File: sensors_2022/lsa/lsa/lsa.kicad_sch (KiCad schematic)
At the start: 18 parts, among them J1 Conn_01x06_Male, U1 LM324

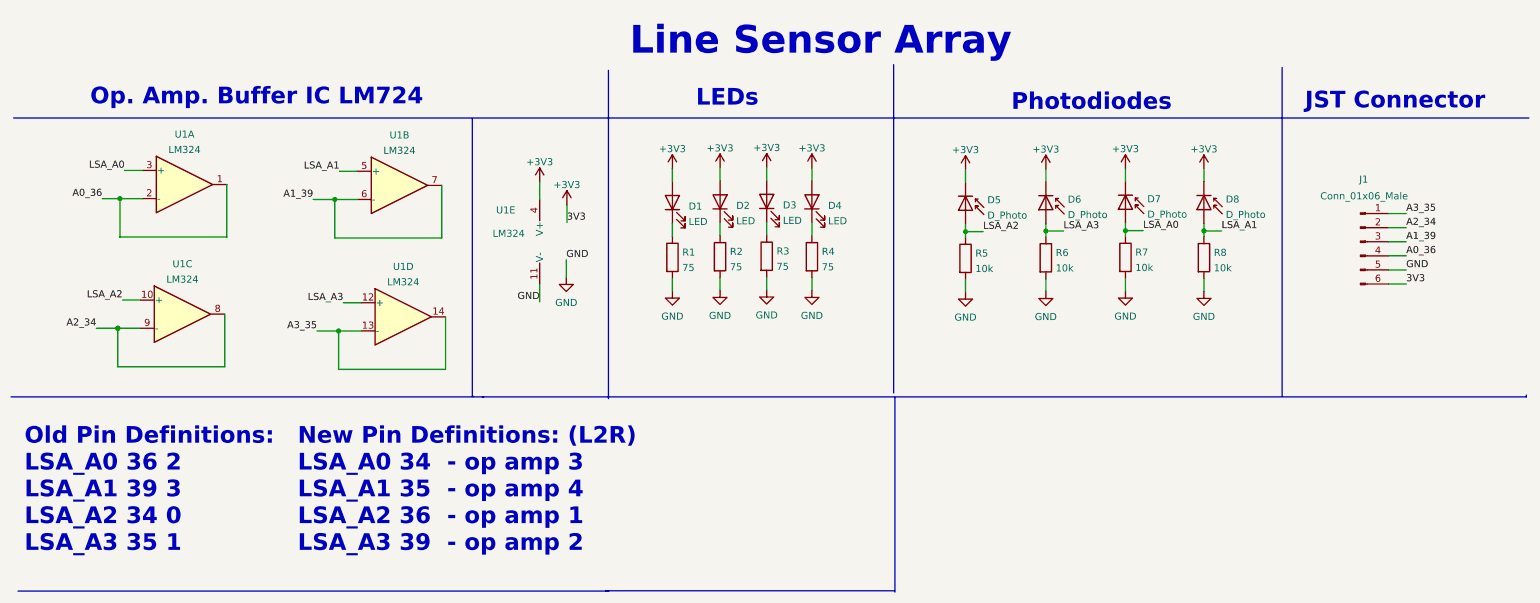
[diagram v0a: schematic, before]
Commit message: add TCRT-5000 base structure to LSA
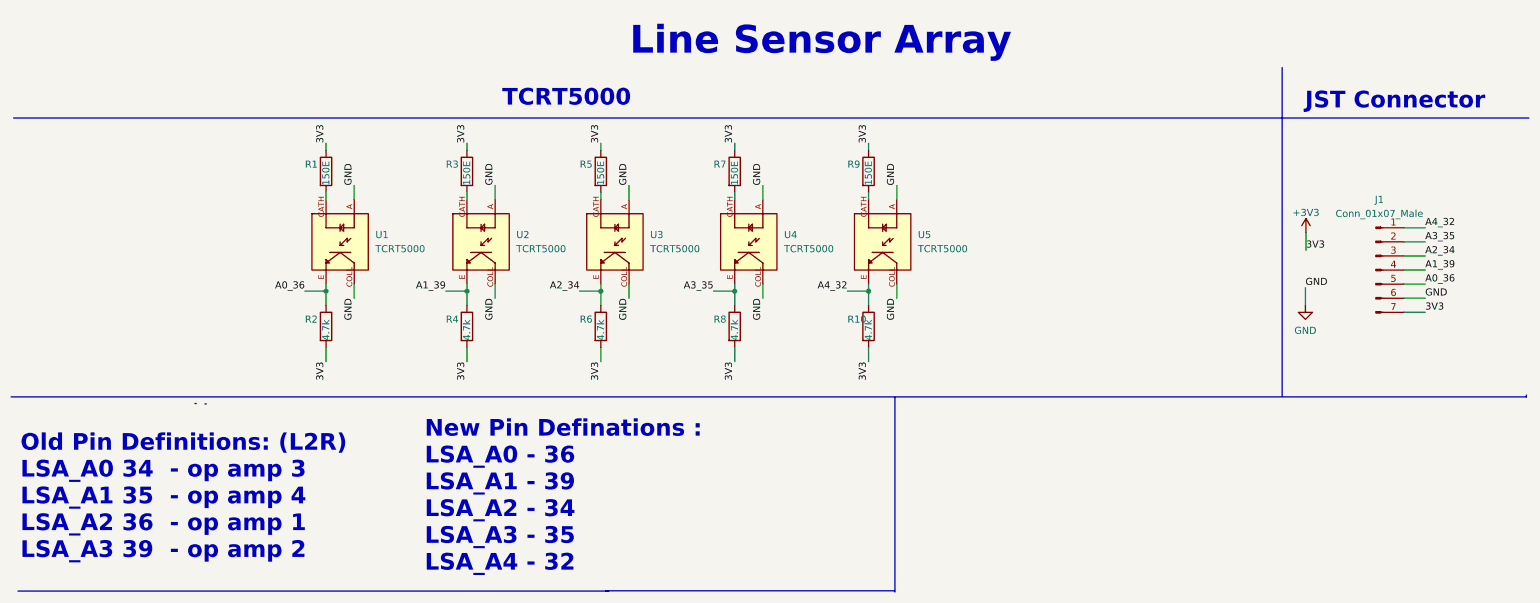
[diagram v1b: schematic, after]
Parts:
- removed D1, D2, D3, D4: LED, LED_THT:LED_D3.0mm, symbol Device:LED
- removed D5, D6, D7, D8: D_Photo, LED_THT:LED_D5.0mm, symbol Device:D_Photo
- removed J1: Conn_01x06_Male, Connector_PinSocket_2.54mm:PinSocket_1x06_P2.54mm_Vertical, symbol Connector:Conn_01x06_Male
- removed U1: LM324, Package_SO:SOIC-14_3.9x8.7mm_P1.27mm, symbol Amplifier_Operational:LM324
- added J1: Conn_01x07_Male, Connector_PinHeader_2.54mm:PinHeader_1x07_P2.54mm_Vertical, symbol Connector:Conn_01x07_Male
- added R10: 4.7k, Resistor_SMD:R_1206_3216Metric_Pad1.30x1.75mm_HandSolder, symbol Device:R
- added R9: 150E, Resistor_SMD:R_1206_3216Metric_Pad1.30x1.75mm_HandSolder, symbol Device:R
- added U1, U2, U3, U4, U5: TCRT5000, TCRT5000:OPTO_TCRT5000, symbol TCRT5000:TCRT5000
- R1, R3: value 75 -> 150E
- R2, R4: value 75 -> 4.7k
- R5, R7: value 10k -> 150E
- R6, R8: value 10k -> 4.7k
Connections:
- net LSA_A0 is gone; now on net +3V3: R7.1
- net LSA_A1 is gone; now on net A3_35: R8.1
- net LSA_A2 is gone; now on net +3V3: R5.1
- net LSA_A3 is gone; now on net A2_34: R6.1
- net +3V3: now also R1.1, R2.2, R3.1, R4.2, R6.2, R8.2, J1.7 (Pin_7), R10.2, R9.1
- net A0_36: now also R2.1, J1.5 (Pin_5), U1.E
- net A1_39: now also R4.1, J1.4 (Pin_4), U2.E
- net A2_34: now also J1.3 (Pin_3), U3.E
- net A3_35: now also J1.2 (Pin_2), U4.E
- net GND: now also J1.6 (Pin_6), U1.A, U1.COLL, U2.A, U2.COLL, U3.A, U3.COLL, U4.A, U4.COLL, U5.A, U5.COLL; no longer R1.2, R2.2, R3.2, R4.2, R5.2, R6.2, R7.2, R8.2
- new net: R9.2, U5.CATH
- new net: R7.2, U4.CATH
- new net: R5.2, U3.CATH
- new net: R1.2, U1.CATH
- new net: R3.2, U2.CATH
- new net A4_32: J1.1 (Pin_1), R10.1, U5.E
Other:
- note added: "New Pin Definations : LSA_A0 - 36 LSA_A1 - 39 LSA_A2 - 34 LSA_A3 - 35 LSA_A4 - 32"
- note added: "Old Pin Definitions: (L2R) LSA_A0 34 - op amp 3 LSA_A1 35 - op amp 4 LSA_A2 36 - op amp 1 LSA_A3 39 - op amp 2"
- note added: "TCRT5000"
- note removed: "LEDs"
- note removed: "New Pin Definitions: (L2R) LSA_A0 34 - op amp 3 LSA_A1 35 - op amp 4 LSA_A2 36 - op amp 1 LSA_A3 39 - op amp 2"
- note removed: "Old Pin Definitions: LSA_A0 36 2 LSA_A1 39 3 LSA_A2 34 0 LSA_A3 35 1"
- note removed: "Op. Amp. Buffer IC LM724"
- note removed: "Photodiodes"
